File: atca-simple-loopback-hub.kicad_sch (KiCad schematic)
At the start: 1 part

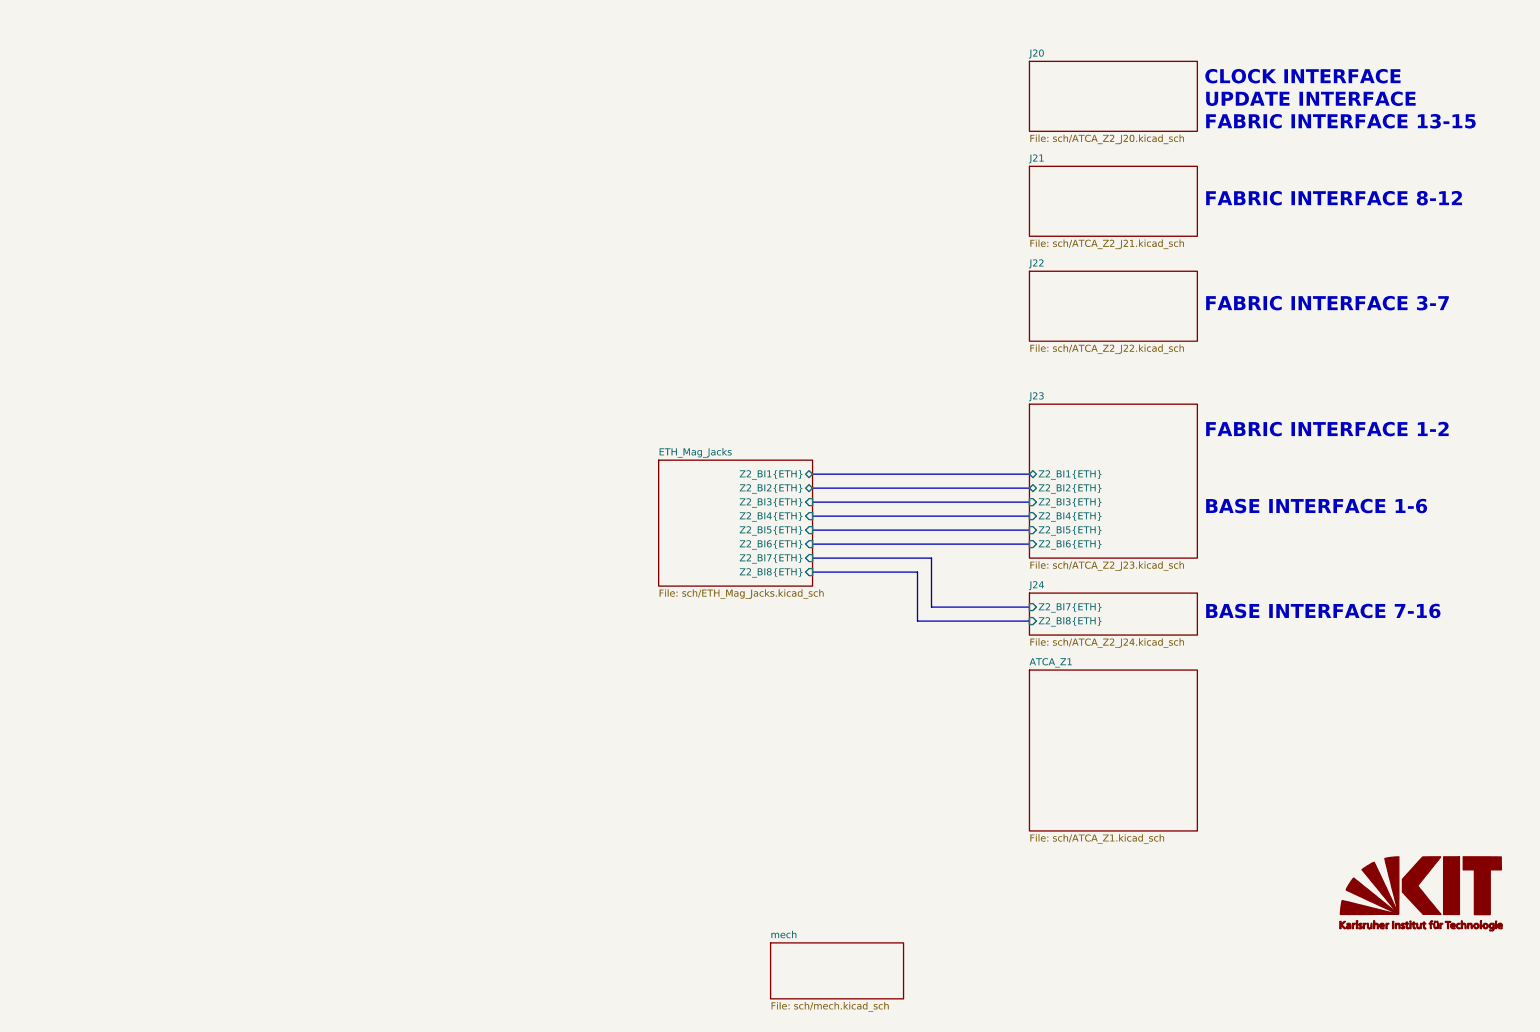
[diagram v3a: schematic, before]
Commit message: adding clks and fiber sheets
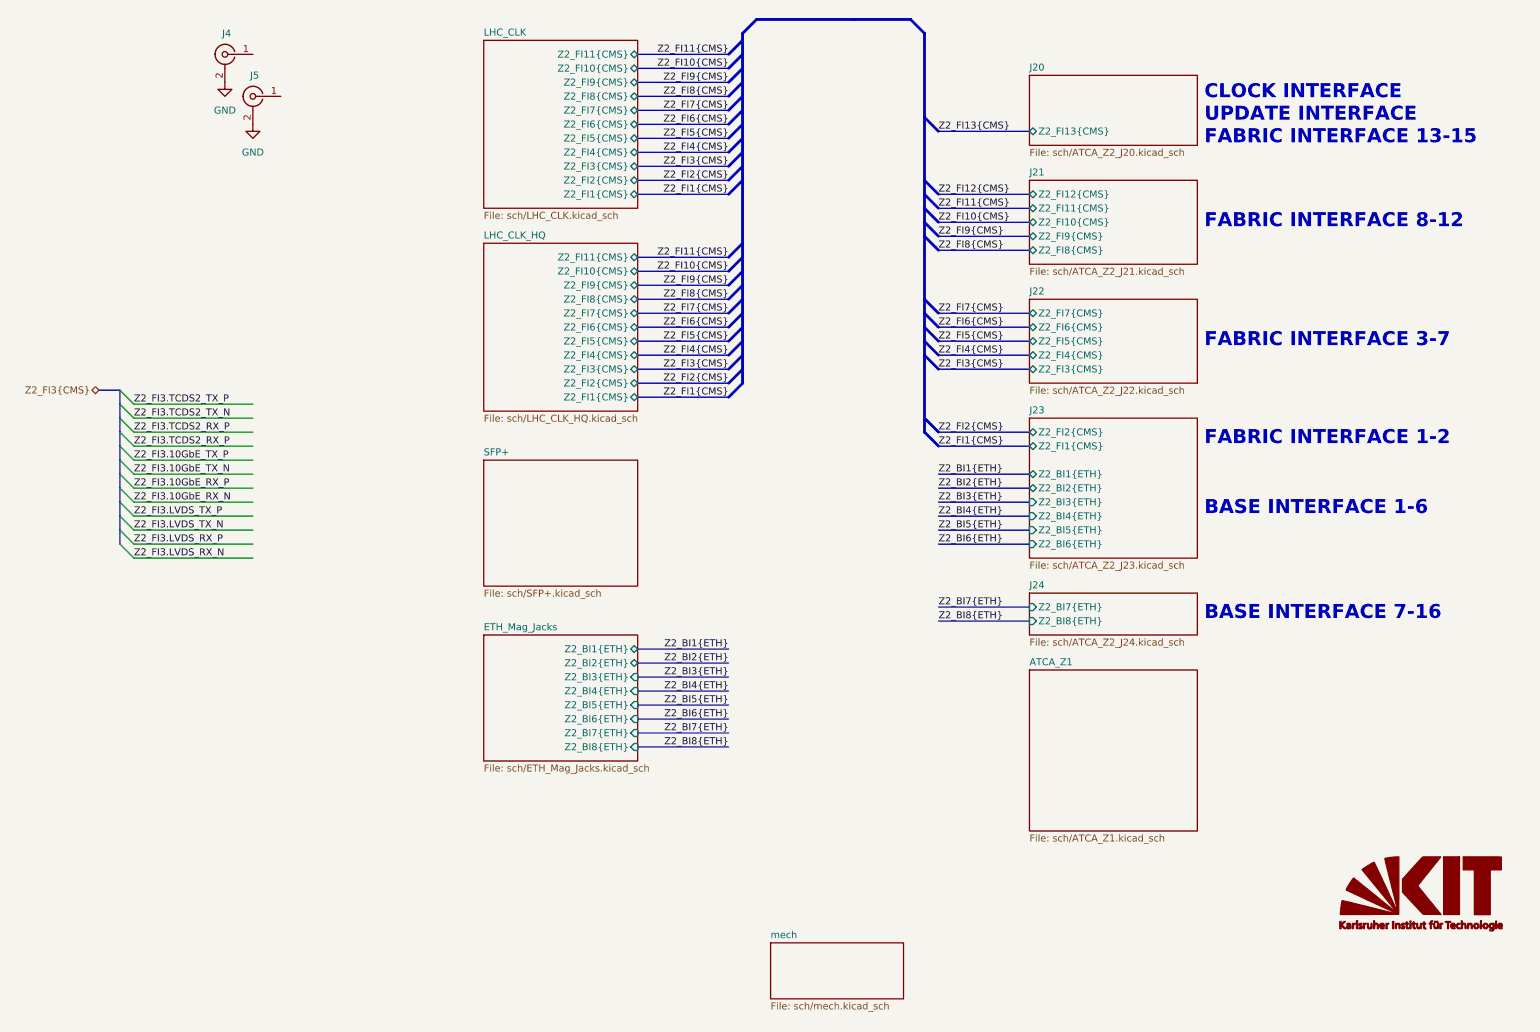
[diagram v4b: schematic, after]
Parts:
- added J4, J5: Conn_Coaxial, symbol Connector:Conn_Coaxial
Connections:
- new net GND: J4.2 (Ext), J5.2 (Ext)
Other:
- added sheet LHC_CLK (sch/LHC_CLK.kicad_sch)
- added sheet LHC_CLK_HQ (sch/LHC_CLK_HQ.kicad_sch)
- added sheet SFP+ (sch/SFP+.kicad_sch)
- sheet J20 ports: added Z2_FI13{CMS}; removed none
- sheet J21 ports: added Z2_FI10{CMS}, Z2_FI11{CMS}, Z2_FI12{CMS}, Z2_FI8{CMS}, Z2_FI9{CMS}; removed none
- sheet J22 ports: added Z2_FI3{CMS}, Z2_FI4{CMS}, Z2_FI5{CMS}, Z2_FI6{CMS}, Z2_FI7{CMS}; removed none
- sheet J23 ports: added Z2_FI1{CMS}, Z2_FI2{CMS}; removed none

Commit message: sfp+ sheet
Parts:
- added J10, J11, J12, J13, J8, J9: Conn_Coaxial, Connector_Coaxial:MMCX_Molex_73415-1471_Vertical, symbol Connector:Conn_Coaxial
- J4, J5: footprint (none) -> Connector_Coaxial:MMCX_Molex_73415-1471_Vertical
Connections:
- net GND: now also J10.2 (Ext), J11.2 (Ext), J12.2 (Ext), J13.2 (Ext), J8.2 (Ext), J9.2 (Ext)
- net Z2_FI3.LVDS_RX_N: now also J13.1 (In)
- net Z2_FI3.LVDS_RX_P: now also J12.1 (In)
- net Z2_FI3.LVDS_TX_N: now also J11.1 (In)
- net Z2_FI3.LVDS_TX_P: now also J10.1 (In)
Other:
- sheet SFP+ ports: added SC_SFP+_1{SFP+}, SC_SFP+_2{SFP+}, Z2_FI3{CMS}; removed none
- moved on the sheet: J5

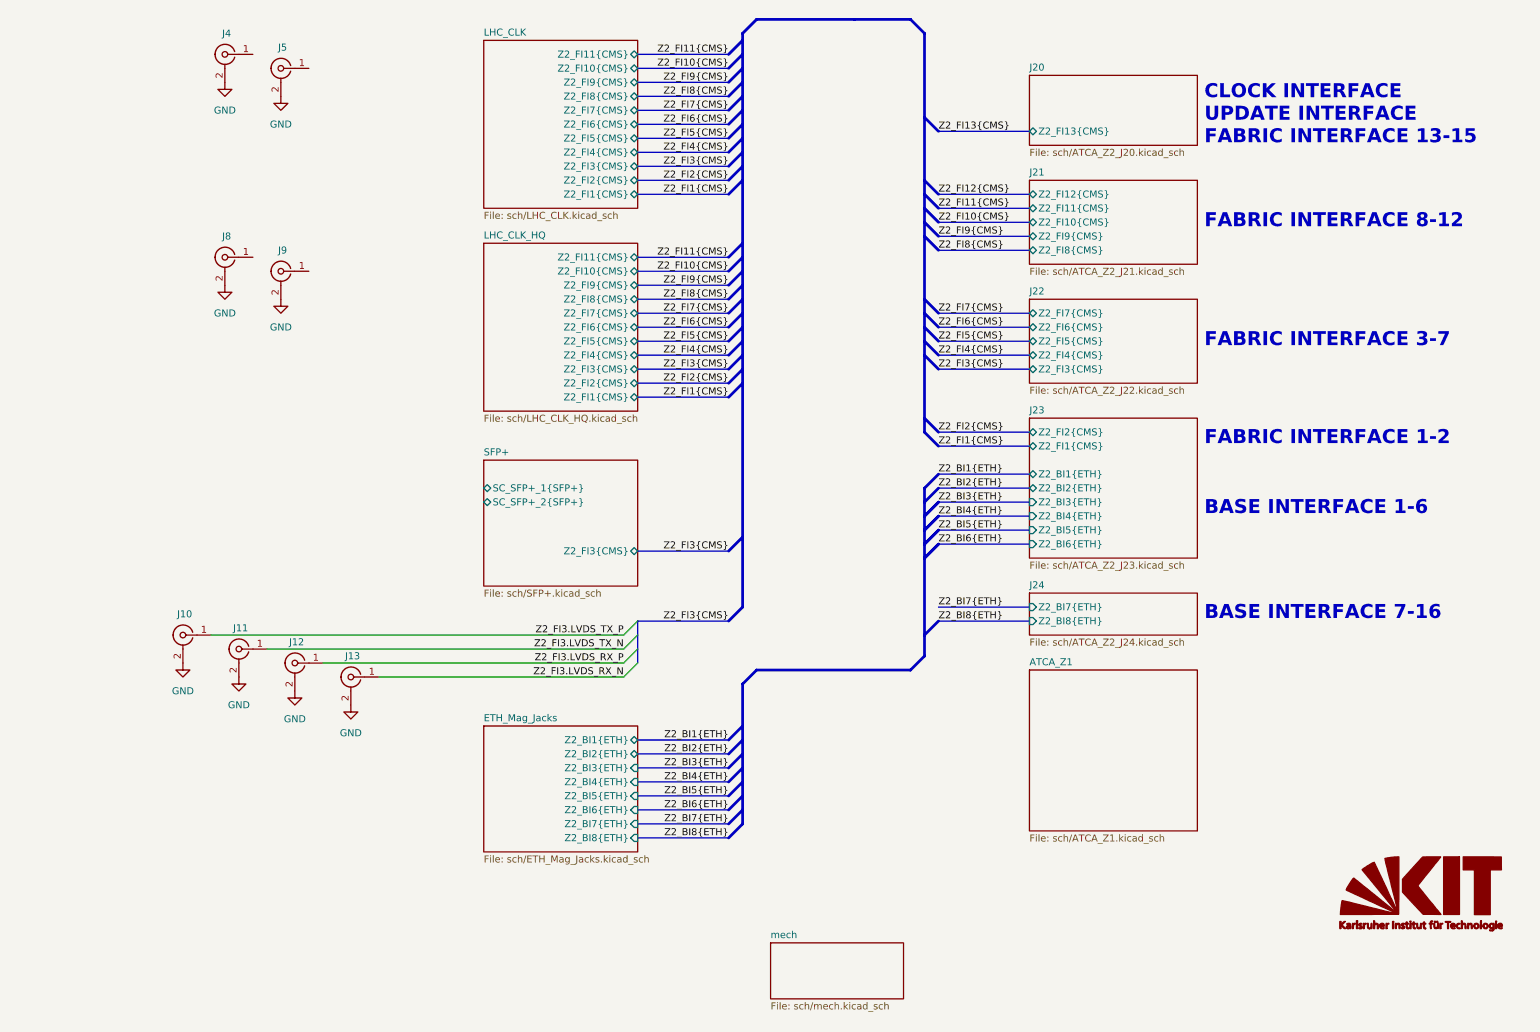
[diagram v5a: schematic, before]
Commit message: work on sc pll and pll sheet
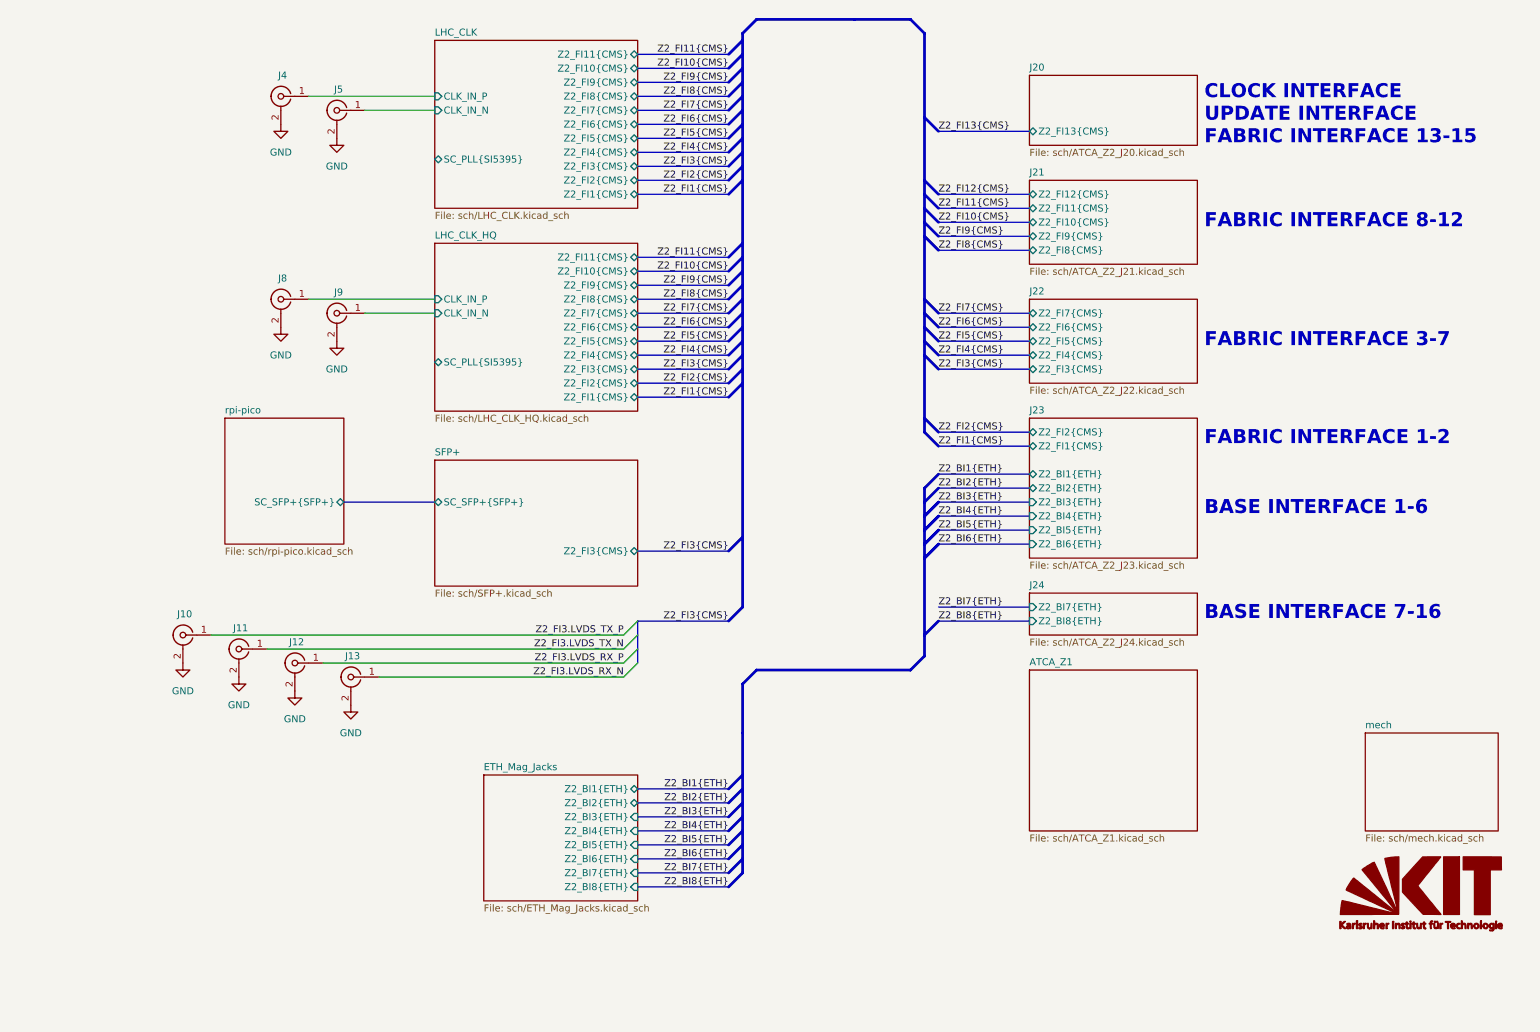
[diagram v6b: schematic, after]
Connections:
- net LHC_CLK_HQ/CLK_IN_P: now reaches J8.1 (In)
- net LHC_CLK/CLK_IN_N: now reaches J5.1 (In)
- net LHC_CLK/CLK_IN_P: now reaches J4.1 (In)
- net LHC_CLK_HQ/CLK_IN_N: now reaches J9.1 (In)
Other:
- added sheet rpi-pico (sch/rpi-pico.kicad_sch)
- sheet LHC_CLK ports: added CLK_IN_N, CLK_IN_P, SC_PLL{SI5395}; removed none
- sheet LHC_CLK_HQ ports: added CLK_IN_N, CLK_IN_P, SC_PLL{SI5395}; removed none
- sheet SFP+ ports: added SC_SFP+{SFP+}; removed SC_SFP+_1{SFP+}, SC_SFP+_2{SFP+}
- moved on the sheet: J4, J5, J8, J9

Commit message: sch work
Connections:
- no-connect marks 0 -> 2
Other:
- added sheet PS_1V8 (sch/PS_1V8.kicad_sch)
- sheet ATCA_Z1 ports: added BUS_N, BUS_P, SC_PIM{PIM400}; removed none
- sheet SFP+ ports: added SC_SFP+_1{SFP+}, SC_SFP+_2{SFP+}; removed SC_SFP+{SFP+}
- sheet rpi-pico ports: added SC_PIM{PIM400}, SC_PLL_1{SI5395}, SC_PLL_2{SI5395}, SC_SFP+_1{SFP+}, SC_SFP+_2{SFP+}; removed SC_SFP+{SFP+}
- moved on the sheet: J10, J11, J12, J13, J4, J5, J8, J9

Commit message: before sch review
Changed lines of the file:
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@@
     )
   )
-  (sheet (at 96.52 142.24) (size 27.94 22.86) (fields_autoplaced)
+  (sheet (at 87.63 142.24) (size 36.83 22.86) (fields_autoplaced)
     (stroke (width 0.1524) (type solid))
     (fill (color 0 0 0 0.0000))
-    (property "Sheetname" "ETH_Mag_Jacks" (at 96.52 141.5284 0)
+    (property "Sheetname" "ETH_Mag_Jacks" (at 87.63 141.5284 0)
       (effects (font (size 1.27 1.27)) (justify left bottom))
     )
-    (property "Sheetfile" "sch/ETH_Mag_Jacks.kicad_sch" (at 96.52 165.6846 0)
+    (property "Sheetfile" "sch/ETH_Mag_Jacks.kicad_sch" (at 87.63 165.6846 0)
       (effects (font (size 1.27 1.27)) (justify left top))
     )
